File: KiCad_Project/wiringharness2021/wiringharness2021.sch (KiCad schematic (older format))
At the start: 38 parts

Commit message: Consolidated harnesslib into main Lukas_Library repo and deleted old
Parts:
- removed U?: MXS1.2, symbol harnesslib:AIMMXL
- removed U?: BOSCH_W0133-1605554, symbol harnesslib:BOSCH_W0133-1605554
- removed U?: BSPD, symbol harnesslib:BSPD
- removed U?: Haltech Connector A, symbol harnesslib:HaltechElite1500A
- removed U?: Haltech Connector B, symbol harnesslib:HaltechElite1500B
- removed U?: PMU16DL, symbol harnesslib:PMU16DL
- removed U?: 91CP16-3 Pressure Sensor, symbol harnesslib:91CP16-3
- removed U?: WirelessTelemetry, symbol harnesslib:WirelessTelemetry
- removed U?: Shift Controller, symbol harnesslib:WirelessTelemetry
- removed U?: Oil Pressure Sensor, symbol harnesslib:91CP16-3
- removed U?: Coolant Temp Sensor, symbol harnesslib:91CP16-3
- removed U?: Crank Position Sensor, symbol harnesslib:91CP16-3
- removed U?: Cam Position Sensor, symbol harnesslib:91CP16-3
- added U?: HaltechElite1500_CONA, symbol Lukas_Library:HaltechElite1500_CONA
- added U?: HaltechElite1500_CONB, symbol Lukas_Library:HaltechElite1500_CONB
- added U?: BOSCH_W0133-1605554, symbol Lukas_Library:BOSCH_W0133-1605554
- added U?: PMU16DL, symbol Lukas_Library:PMU16DL
- added U?: AIM_MXS1.2, symbol Lukas_Library:AIM_MXS1.2
- added U? (x2): WirelessTelemetry, symbol Lukas_Library:WirelessTelemetry
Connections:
- no-connect marks 0 -> 1
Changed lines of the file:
@@
 Comment4 ""
 $EndDescr
-$Comp
-L harnesslib:AIMMXL U?
-U 1 1 6010D67A
-P 10300 1900
-F 0 "U?" H 10878 801 50  0000 L CNN
-F 1 "MXS1.2" H 10878 710 50  0000 L CNN
-F 2 "" H 10300 1900 50  0001 C CNN
-F 3 "" H 10300 1900 50  0001 C CNN
-	1    10300 1900
-	1    0    0    -1
-$EndComp
-$Comp
-L harnesslib:BSPD U?
-U 1 1 6011390C
-P 8000 800
-F 0 "U?" H 8000 1065 50  0000 C CNN
-F 1 "BSPD" H 8000 974 50  0000 C CNN
-F 2 "" H 8050 800 50  0001 C CNN
-F 3 "" H 8050 800 50  0001 C CNN
-	1    8000 800
-	1    0    0    -1
-$EndComp
-$Comp
-L harnesslib:HaltechElite1500A U?
-U 1 1 60115733
-P 1200 4050
-F 0 "U?" H 1200 1250 50  0001 C CNN
-F 1 "Haltech Connector A" H 1200 1350 50  0000 C CNN
-F 2 "" H 1200 4050 50  0001 C CNN
-F 3 "" H 1200 4050 50  0001 C CNN
-	1    1200 4050
-	-1   0    0    1
-$EndComp
-$Comp
-L harnesslib:HaltechElite1500B U?
-U 1 1 6011B413
-P 1200 7750
-F 0 "U?" H 1200 5100 50  0000 C CNN
-F 1 "Haltech Connector B" H 1200 5000 50  0000 C CNN
-F 2 "" H 1200 7750 50  0001 C CNN
-F 3 "" H 1200 7750 50  0001 C CNN
-	1    1200 7750
-	-1   0    0    1
-$EndComp
-$Comp
-L harnesslib:PMU16DL U?
-U 1 1 6011DE74
-P 3650 1200
-F 0 "U?" V 4315 -275 50  0000 C CNN
-F 1 "PMU16DL" V 4224 -275 50  0000 C CNN
-F 2 "" H 3650 1200 50  0001 C CNN
-F 3 "" H 3650 1200 50  0001 C CNN
-	1    3650 1200
-	0    -1   -1   0
-$EndComp
-$Comp
-L harnesslib:WirelessTelemetry U?
-U 1 1 6012DED2
-P 7750 5450
-F 0 "U?" H 7750 5565 50  0000 C CNN
-F 1 "WirelessTelemetry" H 7750 5474 50  0000 C CNN
-F 2 "" H 7750 5450 50  0001 C CNN
-F 3 "" H 7750 5450 50  0001 C CNN
-	1    7750 5450
-	1    0    0    -1
-$EndComp
 Text GLabel 8150 5750 2    50   Input ~ 0
 CANH
@@
 Ignition
 $Comp
-L harnesslib:BOSCH_W0133-1605554 U?
-U 1 1 60112260
-P 3750 5850
-F 0 "U?" H 3725 5965 50  0000 C CNN
-F 1 "BOSCH_W0133-1605554" H 3725 5874 50  0000 C CNN
-F 2 "" H 3750 5850 50  0001 C CNN
-F 3 "" H 3750 5850 50  0001 C CNN
-	1    3750 5850
-	1    0    0    -1
-$EndComp
-$Comp
 L power:GND #PWR?
 U 1 1 601153BF
@@
 	1    9350 4600
 	-1   0    0    1
-$EndComp
-$Comp
-L harnesslib:91CP16-3 U?
-U 1 1 60124857
-P 9500 6000
-F 0 "U?" H 10078 5976 50  0000 L CNN
-F 1 "91CP16-3 Pressure Sensor" H 10078 5885 50  0000 L CNN
-F 2 "" H 9500 6000 50  0001 C CNN
-F 3 "" H 9500 6000 50  0001 C CNN
-	1    9500 6000
-	1    0    0    -1
 $EndComp
 $Comp
@@
 Wire Notes Line
 	7200 2000 7200 3950
-$Comp
-L harnesslib:WirelessTelemetry U?
-U 1 1 601F675A
-P 7750 4250
-F 0 "U?" H 7750 4365 50  0000 C CNN
-F 1 "Shift Controller" H 7750 4274 50  0000 C CNN
-F 2 "" H 7750 4250 50  0001 C CNN
-F 3 "" H 7750 4250 50  0001 C CNN
-	1    7750 4250
-	1    0    0    -1
-$EndComp
 Text GLabel 8150 4550 2    50   Input ~ 0
 CANH
@@
 $EndComp
 $Comp
-L harnesslib:91CP16-3 U?
-U 1 1 601FC026
-P 3500 3100
-F 0 "U?" H 4078 3076 50  0000 L CNN
-F 1 "Oil Pressure Sensor" H 4078 2985 50  0000 L CNN
-F 2 "" H 3500 3100 50  0001 C CNN
-F 3 "" H 3500 3100 50  0001 C CNN
-	1    3500 3100
-	1    0    0    -1
-$EndComp
-$Comp
-L harnesslib:91CP16-3 U?
-U 1 1 601FD8E8
-P 6050 3350
-F 0 "U?" H 6142 2835 50  0000 C CNN
-F 1 "Coolant Temp Sensor" H 6142 2926 50  0000 C CNN
-F 2 "" H 6050 3350 50  0001 C CNN
-F 3 "" H 6050 3350 50  0001 C CNN
-	1    6050 3350
+L Lukas_Library:HaltechElite1500_CONA U?
+U 1 1 601233F5
+P 1200 4050
+F 0 "U?" H 1213 1235 50  0000 C CNN
+F 1 "HaltechElite1500_CONA" H 1213 1326 50  0000 C CNN
+F 2 "" H 1200 4050 50  0001 C CNN
+F 3 "" H 1200 4050 50  0001 C CNN
+	1    1200 4050
 	-1   0    0    1
 $EndComp
-$Comp
-L harnesslib:91CP16-3 U?
-U 1 1 601FF714
-P 6050 4250
-F 0 "U?" H 6142 3735 50  0000 C CNN
-F 1 "Crank Position Sensor" H 6142 3826 50  0000 C CNN
-F 2 "" H 6050 4250 50  0001 C CNN
-F 3 "" H 6050 4250 50  0001 C CNN
-	1    6050 4250
+NoConn ~ 2800 3900
+$Comp
+L Lukas_Library:HaltechElite1500_CONB U?
+U 1 1 60127D4D
+P 1200 7750
+F 0 "U?" H 1167 4885 50  0000 C CNN
+F 1 "HaltechElite1500_CONB" H 1167 4976 50  0000 C CNN
+F 2 "" H 1200 7750 50  0001 C CNN
+F 3 "" H 1200 7750 50  0001 C CNN
+	1    1200 7750
 	-1   0    0    1
 $EndComp
 $Comp
-L harnesslib:91CP16-3 U?
-U 1 1 60200D45
-P 4800 4100
-F 0 "U?" H 5378 4076 50  0000 L CNN
-F 1 "Cam Position Sensor" H 4400 4400 50  0000 L CNN
-F 2 "" H 4800 4100 50  0001 C CNN
-F 3 "" H 4800 4100 50  0001 C CNN
-	1    4800 4100
-	1    0    0    -1
-$EndComp
+L Lukas_Library:BOSCH_W0133-1605554 U?
+U 1 1 6012B145
+P 3750 5850
+F 0 "U?" H 3725 5965 50  0000 C CNN
+F 1 "BOSCH_W0133-1605554" H 3725 5874 50  0000 C CNN
+F 2 "" H 3750 5850 50  0001 C CNN
+F 3 "" H 3750 5850 50  0001 C CNN
+	1    3750 5850
+	1    0    0    -1
+$EndComp
+$Comp
+L Lukas_Library:PMU16DL U?
+U 1 1 6012D012
+P 3650 1200
+F 0 "U?" V 4315 -217 50  0000 C CNN
+F 1 "PMU16DL" V 4224 -217 50  0000 C CNN
+F 2 "" H 3650 1200 50  0001 C CNN
+F 3 "" H 3650 1200 50  0001 C CNN
+	1    3650 1200
+	0    -1   -1   0
+$EndComp
+$Comp
+L Lukas_Library:AIM_MXS1.2 U?
+U 1 1 601304AB
+P 10300 1900
+F 0 "U?" H 10878 801 50  0000 L CNN
+F 1 "AIM_MXS1.2" H 10878 710 50  0000 L CNN
+F 2 "" H 10300 1900 50  0001 C CNN
+F 3 "" H 10300 1900 50  0001 C CNN
+	1    10300 1900
+	1    0    0    -1
+$EndComp
+$Comp
+L Lukas_Library:WirelessTelemetry U?
+U 1 1 60133BA6
+P 7750 4250
+F 0 "U?" H 7750 4365 50  0000 C CNN
+F 1 "WirelessTelemetry" H 7750 4274 50  0000 C CNN
+F 2 "" H 7750 4250 50  0001 C CNN
+F 3 "" H 7750 4250 50  0001 C CNN
+	1    7750 4250
+	1    0    0    -1
+$EndComp
+$Comp
+L Lukas_Library:WirelessTelemetry U?
+U 1 1 60134F69
+P 7750 5450
+F 0 "U?" H 7750 5565 50  0000 C CNN
+F 1 "WirelessTelemetry" H 7750 5474 50  0000 C CNN
+F 2 "" H 7750 5450 50  0001 C CNN
+F 3 "" H 7750 5450 50  0001 C CNN
+	1    7750 5450
+	1    0    0    -1
+$EndComp

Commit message: Progress on harness
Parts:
- removed SW? (x2): MAIN SHUTOFF, symbol Switch:SW_DIP_x01
- added M?: Water Pump, symbol Motor:Motor_DC
- added SW?: BRAKE OVERTRAVEL, symbol Switch:SW_DIP_x01
- added U?: Cam Position, symbol Lukas_Library:VR_Sensor
- added U?: Crank Position, symbol Lukas_Library:VR_Sensor
- added U?: Oil Pres., symbol Lukas_Library:Generic_5v_Sensor
- added U?: Coolant Temp, symbol Lukas_Library:Generic_5v_Sensor
- added U?: Air Temp, symbol Lukas_Library:Generic_5v_Sensor
- added U?: Fuel Pressure Sensor, symbol Lukas_Library:Generic_5v_Sensor
- added U?: BSPD, symbol Lukas_Library:BSPD
- added U?: Air Pres, symbol Lukas_Library:Generic_5v_Sensor
- added U?: Accel. Pedal Pos 1, symbol Lukas_Library:Generic_5v_Sensor
- added U?: Accel. Pedal Pos 2, symbol Lukas_Library:Generic_5v_Sensor
- added U?: Brake Pressure, symbol Lukas_Library:Generic_5v_Sensor
- added U?: BOSCH_280750149, symbol Lukas_Library:BOSCH_280750149
- added U?: Knock Sensor, symbol Lukas_Library:VR_Sensor
- BZ?: value Fuel Injector -> Fuel Injector 1
- BZ?: value Fuel Injector -> Fuel Injector 2
- BZ?: value Fuel Injector -> Fuel Injector 3
- BZ?: value Fuel Injector -> Fuel Injector 4
- M?: value Fuel Pump -> Starter Motor
- SW?: value MAIN SHUTOFF -> DRIVER KILL
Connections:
- net +12v: now also U?.4 (RELAY), U?.5 (+12v)
- net FUELPRES: now also U?.2 (Out)
- net FUELPUMP_SUPPLY: now also U?.26 (O3)
- net GND: now also M?.2 (-), M?.2 (-), U?.3 (GND), U?.3 (GND), U?.3 (GND), U?.3 (GND), U?.3 (GND), U?.3 (GND), U?.3 (GND), U?.3 (GND), U?.6 (GND)
- net APP1: now reaches U?.16 (AVI2)
- net APP1: now also U?.1 (SENS1), U?.2 (Out)
- net TPS2: now reaches U?.17 (AVI3)
- net TPS2: now also U?.5 (TPS2)
- net ETC_+5v: now reaches U?.7 (+5V_Sensor_Supply)
- net ETC_+5v: now also U?.1 (+5v), U?.1 (+5v), U?.3 (Sensor_+5v)
- net ENG_+5: now reaches U?.8 (+5V_Sensor_Supply)
- net ENG_+5: now also U?.1 (+5v), U?.1 (+5v), U?.1 (+5v), U?.1 (+5v)
- net CRANK+: now reaches U?.1 (CRANK+)
- net CRANK+: now also U?.1 (+)
- net AIRPRES: now reaches U?.12 (AVI6)
- net AIRPRES: now also U?.2 (Out)
- net OILPRES: now reaches U?.13 (AVI1)
- net OILPRES: now also U?.2 (Out)
- net CAM+: now reaches U?.2 (CAM+)
- net CAM+: now also U?.1 (+)
- net KNOCK+: now reaches U?.21 (KNOCK1)
- net KNOCK+: now also U?.1 (+)
- net ETCMOTOR+: now reaches U?.25 (DBW1)
- net ETCMOTOR+: now also U?.4 (MOTOR+)
- net ETCMOTOR-: now reaches U?.26 (DBW2)
- net ETCMOTOR-: now also U?.1 (MOTOR-)
- net AIRTEMP: now reaches U?.3 (AVI7)
- net AIRTEMP: now also U?.2 (Out)
- net CLNTTEMP: now reaches U?.4 (AVI8)
- net CLNTTEMP: now also U?.2 (Out)
- net CRANK-: now reaches U?.5 (CRANK-)
- net CRANK-: now also U?.2 (-)
- net CAM-: now reaches U?.6 (CAM-)
- net CAM-: now also U?.2 (-)
- net STARTER: now reaches U?.12 (O5)
- net STARTER: now also M?.1 (+), U?.2 (O12), U?.28 (O16)
- net WATERPUMP: now reaches U?.38 (O1)
- net WATERPUMP: now also M?.1 (+)
- net CAR_ON: now reaches U?.7 (+12V_SW)
- net CAR_ON: now also SW?.2
- net UPSHIFT: now reaches U?.1 (Analog_Input_5)
- net UPSHIFT: now also SW?.2
- net START: now reaches U?.10 (Analog_Input_8)
- net START: now also SW?.2
- net DOWNSHIFT: now reaches U?.5 (Analog_Input_6)
- net DOWNSHIFT: now also SW?.2
- net NEUTRAL: now reaches U?.6 (Analog_Input_7)
- net NEUTRAL: now also SW?.2
- net DRVKILL: now reaches SW?.1
- net DRVKILL: now also U?.3 (RELAY)
- net OT_KILL: now reaches SW?.2
- net OT_KILL: now also SW?.1
- net COILPACK_SUPPLY renamed COILS+
- new net APP2: U?.2 (Out)
- new net BRAKEPRES: U?.2 (Out), U?.2 (SENS2)
- no-connect marks 1 -> 5
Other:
- note added: "Electronic Throttle Body"
- note added: "Pedal Box"
- moved on the sheet: BT?, D?, E?, F?, M?, SW?, T?, U?

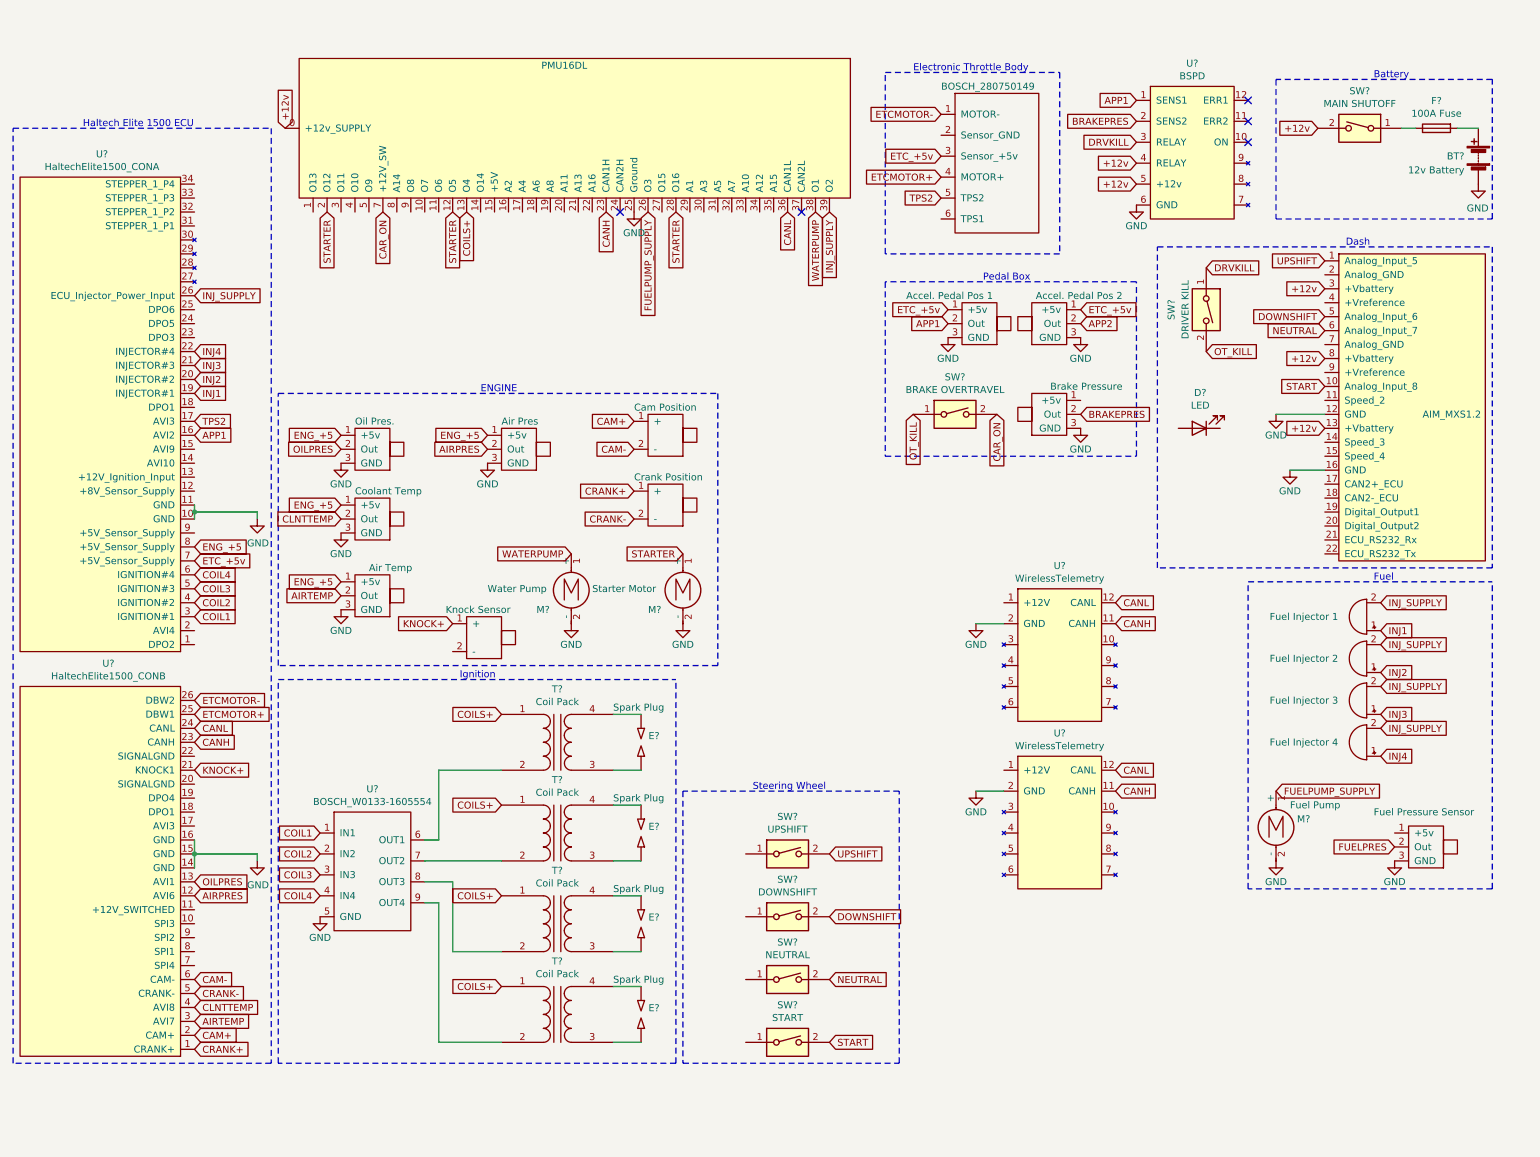
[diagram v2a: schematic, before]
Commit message: Shift controller added and improved organization
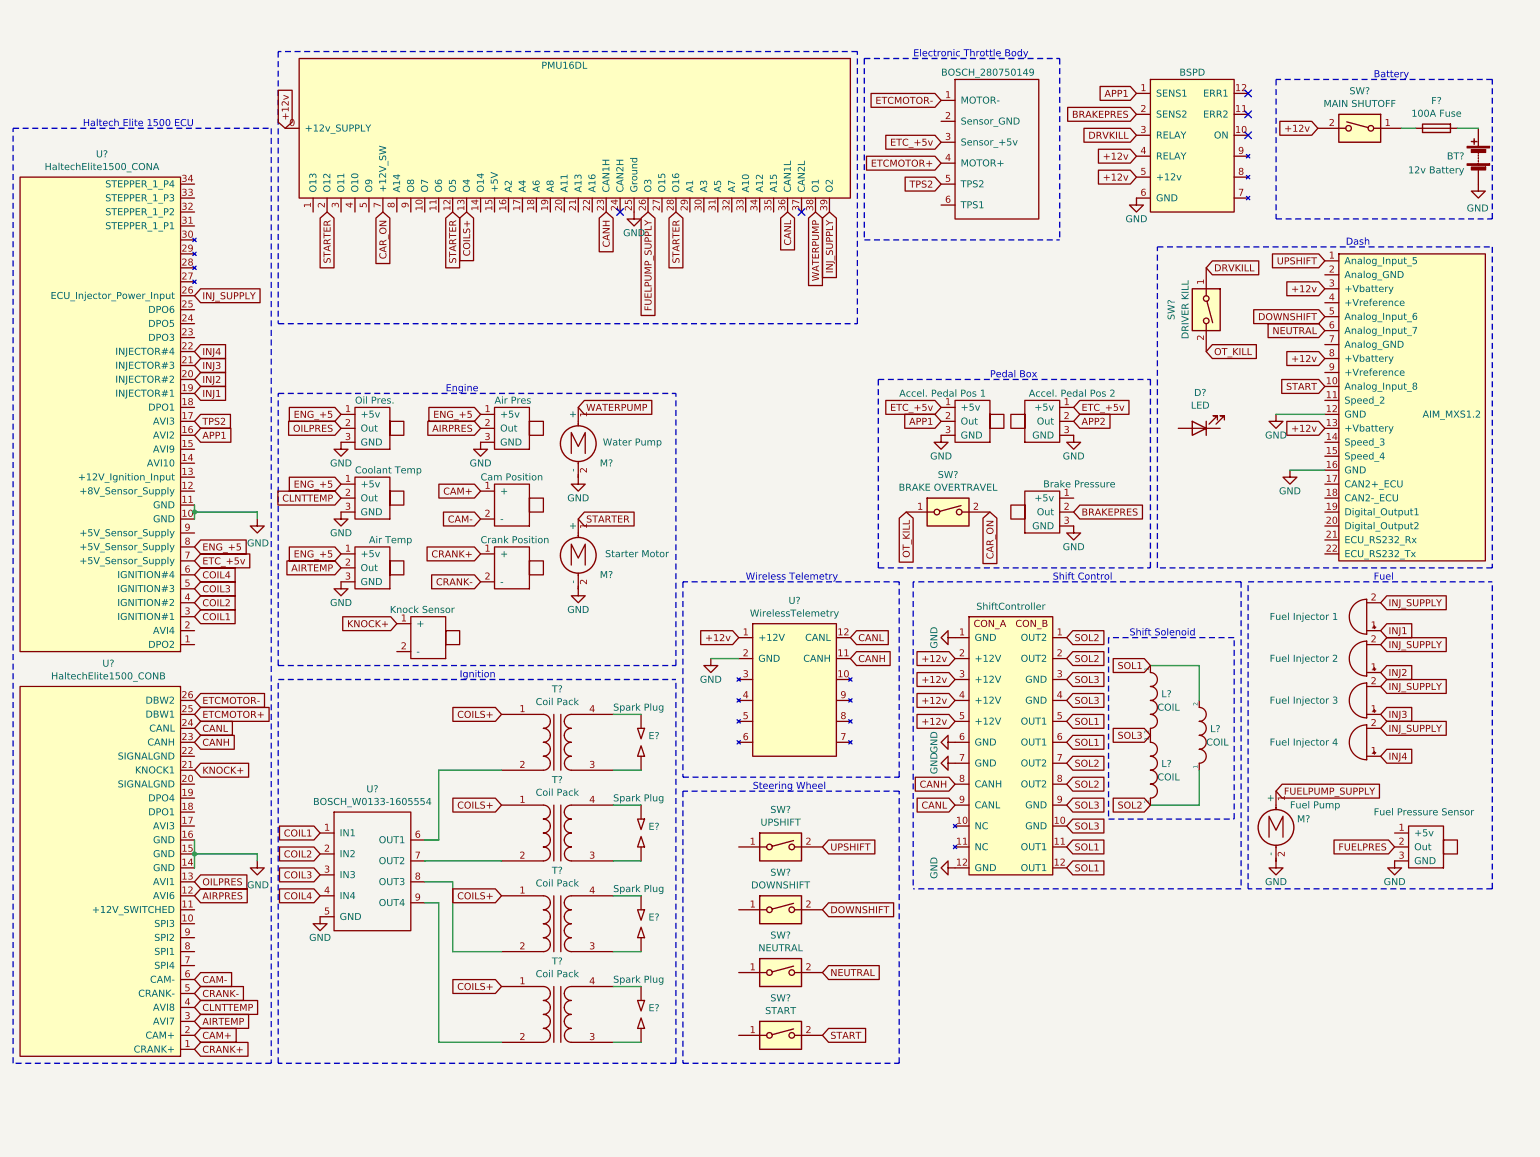
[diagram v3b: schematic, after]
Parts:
- removed U?: WirelessTelemetry, symbol Lukas_Library:WirelessTelemetry
- added L? (x3): COIL, symbol pspice:INDUCTOR
- added U?: ShiftController, symbol Lukas_Library:ShiftController
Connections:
- net +12v: now also U?.1 (+12V), U?.2 (OUT2), U?.3 (GND), U?.4 (GND), U?.5 (OUT1)
- net CANH: now also U?.8 (OUT2)
- net CANL: now also U?.9 (GND)
- net GND: now also U?.1 (OUT2), U?.12 (OUT1), U?.6 (OUT1), U?.7 (OUT2)
- new net SOL1: L?.1, L?.2, U?.11 (OUT1), U?.12 (OUT1), U?.5 (OUT1), U?.6 (OUT1)
- new net SOL2: L?.1, L?.2, U?.1 (OUT2), U?.2 (OUT2), U?.7 (OUT2), U?.8 (OUT2)
- new net SOL3: L?.1, L?.2, U?.10 (NC), U?.3 (GND), U?.4 (GND), U?.9 (GND)
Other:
- note added: "Engine"
- note added: "Shift Control"
- note added: "Shift Solenoid"
- note added: "Wireless Telemetry"
- note removed: "ENGINE"
- moved on the sheet: M?, SW?, U?

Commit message: Finished revision 1 and exported pdf drawing
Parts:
- added D1: LED, symbol Device:LED
- added M3, M4: FAN, symbol Motor:Motor_DC
- added R1, R2: 220, symbol Device:R_US
- U9: renamed from U?; value Air Pres -> Air Pressure
- gave numbers to parts that had none: 47
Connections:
- net labels added: BRAKELIGHT, ECU_PWR, RADFAN1, RADFAN2, SIGNALGND, TPS1
- wire segments 35 -> 46
- no-connect marks 5 -> 56
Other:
- note added: "Brake Light"
- note added: "Brake System Plausability Device"
- note added: "Neutral Light"
- note added: "Power Management Unit"
- note added: "Radiator Fans"
- moved on the sheet: D2, M1, M2, SW6
